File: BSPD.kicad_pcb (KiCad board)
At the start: 2 copper layers, 96.5 x 35.6 mm, 46 parts, among them J1 Conn_02x04_Odd_Even, J2 Screw_Terminal_01x02, K1 RT444012, Q1 IRLML2502, U1 AZ1117-5.0, U2 LM2901D, U3 LM2901D

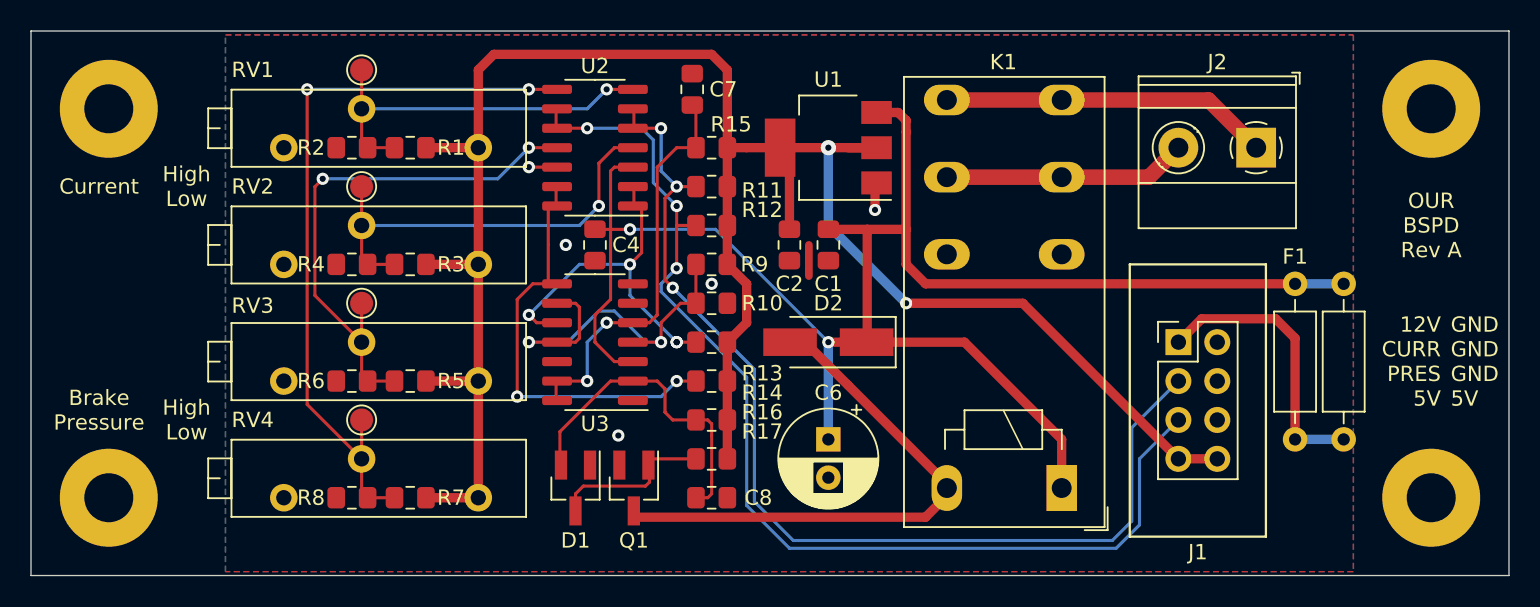
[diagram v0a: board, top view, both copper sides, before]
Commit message: add logo
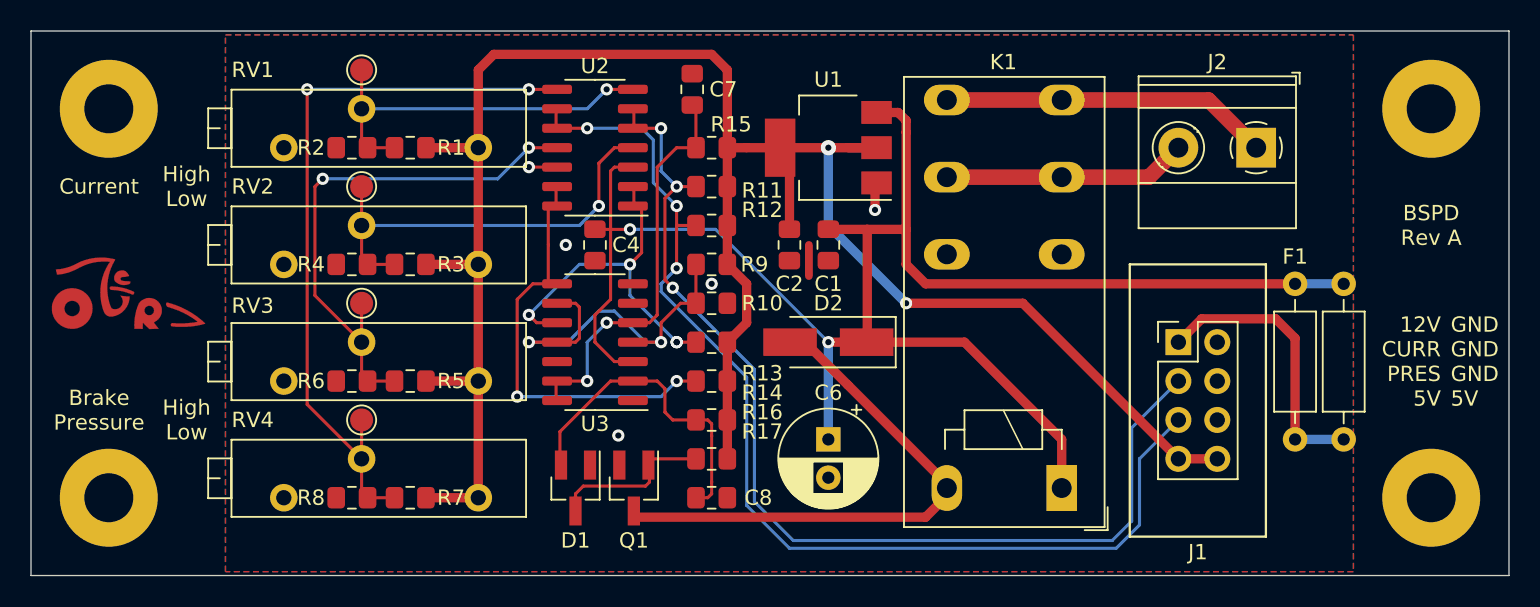
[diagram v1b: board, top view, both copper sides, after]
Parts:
- added G***: LOGO, project:OUR-Logo, F.Cu at (69.8, 81.3)
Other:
- board text added: "BSPD Rev A"
- board text removed: "OUR BSPD Rev A"

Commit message: update schematics
Change regulator to ZLDO1117
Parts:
- U1: value AZ1117-5.0 -> ZLDO1117G50
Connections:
- U1 pad 4: +5V -> (no net)
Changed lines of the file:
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@@
-(kicad_pcb (version 20171130) (host pcbnew 5.1.4)
+(kicad_pcb (version 20171130) (host pcbnew 5.1.5)
   (general
     (thickness 1.6)
@@
       (effects (font (size 1 1) (thickness 0.15)))
     )
-    (fp_text value AZ1117-5.0 (at 0 4.5) (layer F.Fab)
+    (fp_text value ZLDO1117G50 (at 0 4.5) (layer F.Fab)
       (effects (font (size 1 1) (thickness 0.15)))
     )
@@
     (fp_line (start -1.85 3.35) (end 1.85 3.35) (layer F.Fab) (width 0.1))
     (fp_line (start 1.85 -3.35) (end 1.85 3.35) (layer F.Fab) (width 0.1))
-    (pad 4 smd rect (at 3.15 0 180) (size 2 3.8) (layers F.Cu F.Paste F.Mask)
-      (net 3 +5V))
+    (pad 4 smd rect (at 3.15 0 180) (size 2 3.8) (layers F.Cu F.Paste F.Mask))
     (pad 2 smd rect (at -3.15 0 180) (size 2 1.5) (layers F.Cu F.Paste F.Mask)
       (net 3 +5V))
@@
       (effects (font (size 1 1) (thickness 0.15)))
     )
-    (fp_text value 10uF (at -0.635 2.54 180) (layer F.Fab)
+    (fp_text value 10uF (at 1.81 0.02 180) (layer F.Fab)
       (effects (font (size 1 1) (thickness 0.15)))
     )
@@
       (effects (font (size 1 1) (thickness 0.15)))
     )
-    (fp_text value 1uF (at 0 2.54 180) (layer F.Fab)
-      (effects (font (size 1 1) (thickness 0.15)))
-    )
+    (fp_text value 1uF (at 0.03 2.13 180) (layer F.Fab)
+      (effects (font (size 1 1) (thickness 0.15)))
+    )
